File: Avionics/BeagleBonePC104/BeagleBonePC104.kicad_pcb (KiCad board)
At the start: 2 copper layers, 4 parts

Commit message: Ian Goldberg - Finished the footprint for the BeagleBonePCI104 Motherboard
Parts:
- added U2: ~, PCI104Connector:PCI104ConnectorAttempt#2H1, F.Cu at (80.0, 170.0)
- added U4: ~, PCI104Connector:PCI104ConnectorAttempt#2H2, F.Cu at (80.0, 170.0)
- moved U1 80.1 mm to (170.1, 90.8), turned to 180 degrees
- moved R1 63.2 mm to (113.0, 150.0)
- moved R2 51.1 mm to (126.5, 150.0)
- moved U3 21.6 mm to (110.1, 147.9), turned to 180 degrees
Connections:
- U1 pad 25: /GPIO3_21 -> /CAN_SLNT
- U3 pad 1: (no net) -> /3V3
- U3 pad 2: (no net) -> GND
- U3 pad 3: (no net) -> /CAN1_TX
- U3 pad 4: (no net) -> /CAN1_RX
- U3 pad 5: (no net) -> /CAN_SLNT
- U3 pad 6: (no net) -> /CAN_H
- U3 pad 7: (no net) -> /CAN_L
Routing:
- net GND: track 0.00 -> 2.54 mm
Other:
- board outline added: 90.2 x 95.9 mm

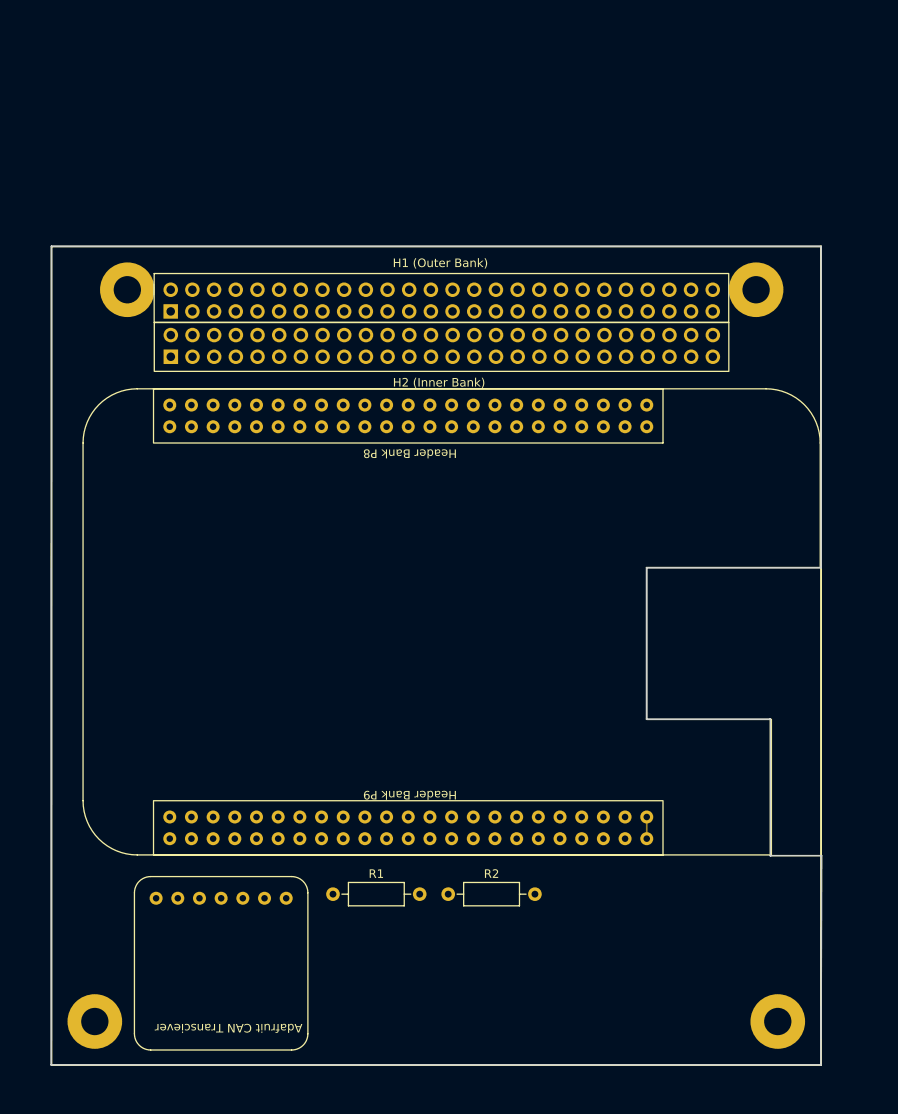
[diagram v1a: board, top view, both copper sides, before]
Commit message: Ian Goldberg - Finally finished the breakout board for the BeagleBone Black. Hoping to order the connectors soon and then asemble it.
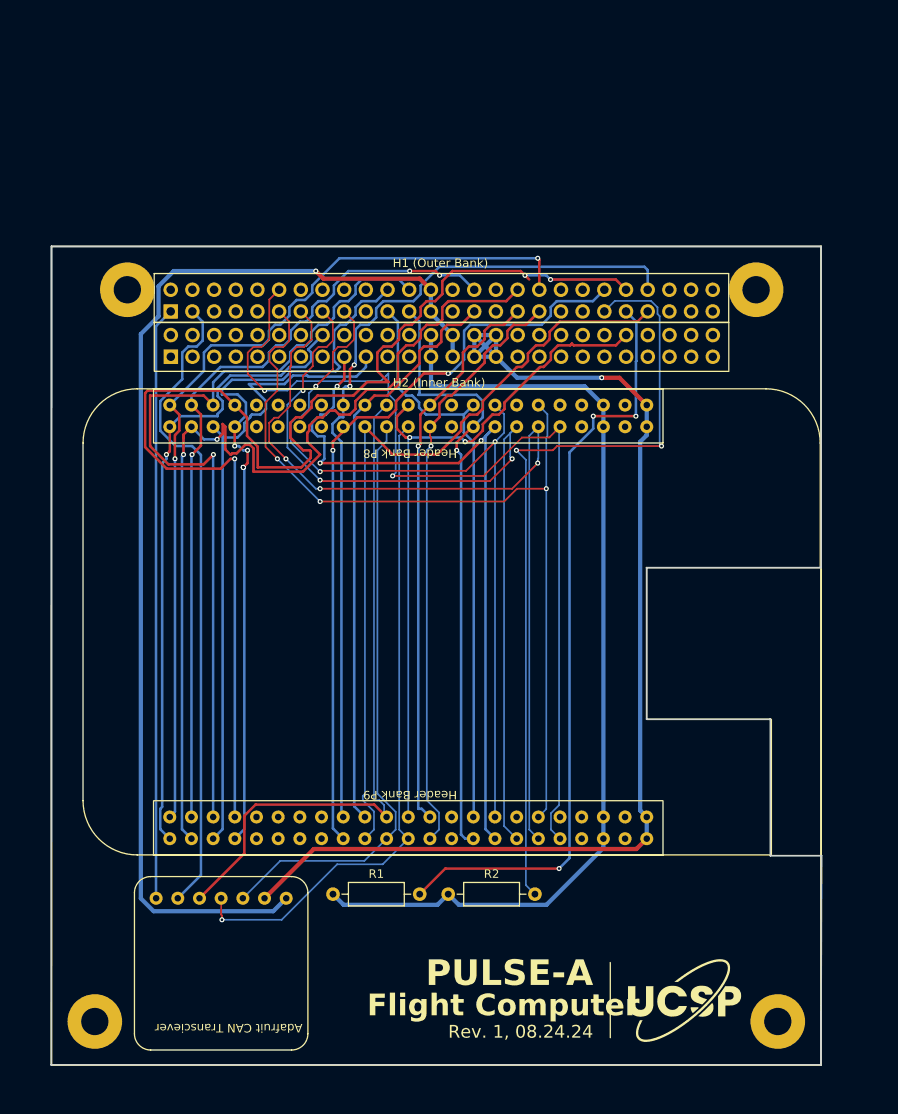
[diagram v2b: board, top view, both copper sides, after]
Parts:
- added G***: LOGO, LOGO, F.Cu at (154.0, 162.5)
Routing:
- net /GPIO2_12: track 0.00 -> 146.9 mm, vias 0 -> 3
- net GND: track 2.54 -> 136.5 mm, vias 0 -> 1
- net /3V3: track 0.00 -> 133.5 mm, vias 0 -> 1
- net /5V: track 0.00 -> 115.0 mm
- net /SYS_RESETn: track 0.00 -> 113.7 mm, vias 0 -> 2
- net /GPIO2_9: track 0.00 -> 112.7 mm, vias 0 -> 2
- net /GPIO1_12: track 0.00 -> 107.0 mm, vias 0 -> 3
- net /GPIO2_6: track 0.00 -> 106.1 mm, vias 0 -> 2
- net /GPIO1_13: track 0.00 -> 104.1 mm, vias 0 -> 3
- net /GPIO1_26: track 0.00 -> 102.0 mm, vias 0 -> 3
- net /GPIO2_23: track 0.00 -> 101.4 mm, vias 0 -> 2
- net /GPIO2_10: track 0.00 -> 98.9 mm, vias 0 -> 1
- net /GPIO1_15: track 0.00 -> 95.7 mm, vias 0 -> 3
- net /I2C_SDA: track 0.00 -> 93.6 mm, vias 0 -> 2
- net /GPIO2_24: track 0.00 -> 92.9 mm
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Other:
- board text added: "Flight Computer"
- board text added: "PULSE-A"
- board text added: "Rev. 1, 08.24.24"

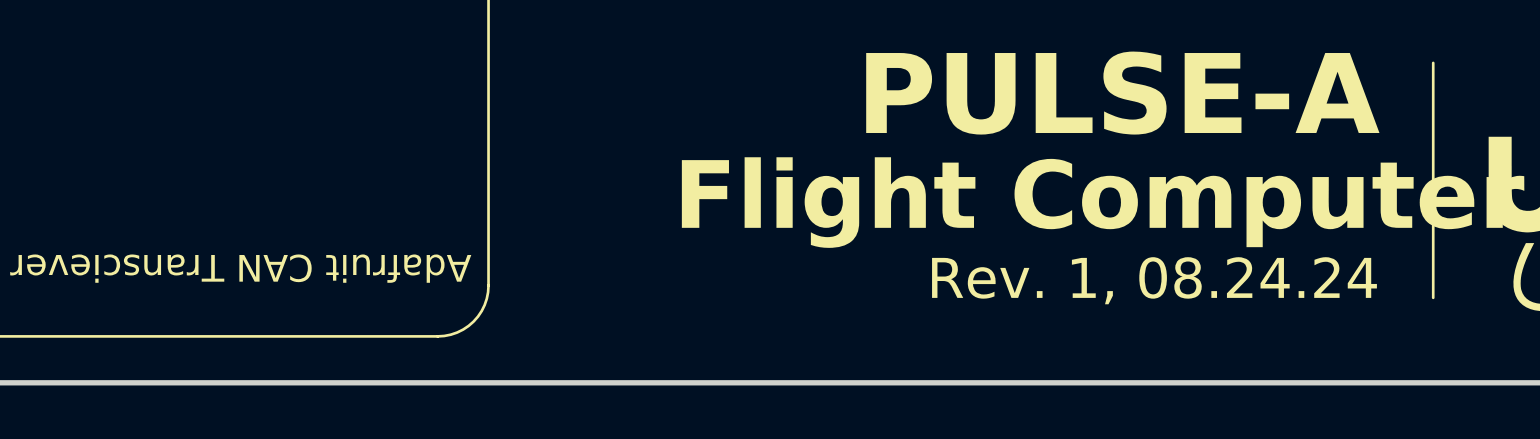
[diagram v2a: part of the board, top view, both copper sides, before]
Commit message: Ian Goldberg - pushed a correction to the BeagleBone Motherboard
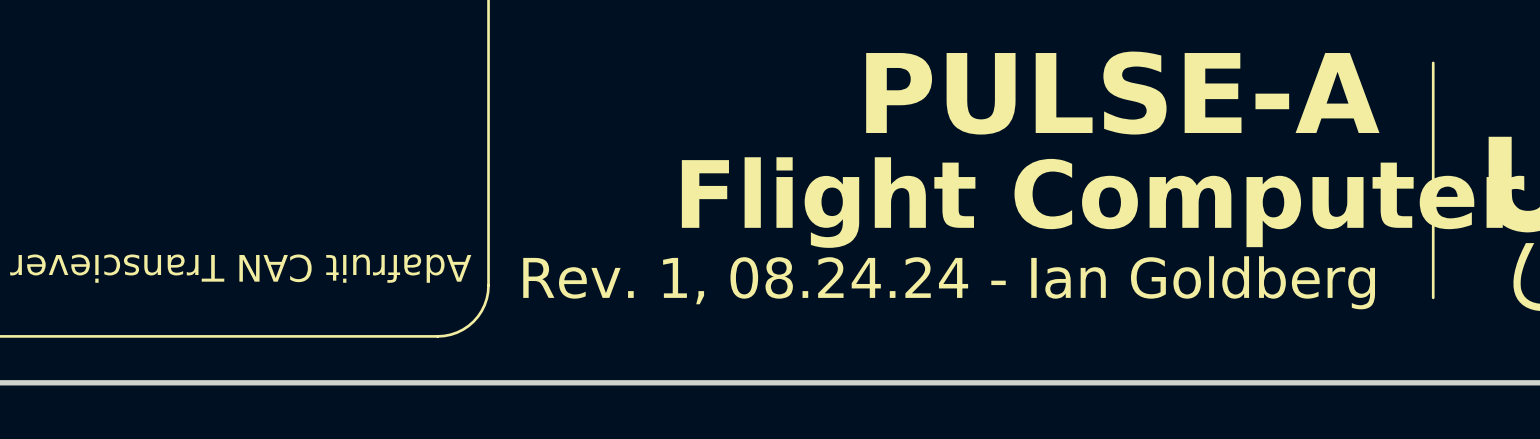
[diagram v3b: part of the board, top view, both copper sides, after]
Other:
- board text added: "Rev. 1, 08.24.24 - Ian Goldberg"
- board text removed: "Rev. 1, 08.24.24"

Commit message: Finally finished the BeagleBone Motherboard
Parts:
- moved G*** 1.12 mm to (154.5, 161.5)
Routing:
- net /GPIO2_6: track 106.1 -> 104.4 mm
- net /GPIO2_12: track 146.9 -> 145.8 mm
- net /GPIO2_13: vias 4 -> 3
- added copper zone on B.Cu, net GND
- added copper zone on F.Cu, net GND
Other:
- outline, holes or cut-outs redrawn
- board text added: "Rev. 1 - 08.24.24 - Ian Goldberg"
- board text added: "{dblquote}Do or do not, there is no try{dblquote} - Yoda"
- board text removed: "Rev. 1, 08.24.24 - Ian Goldberg"

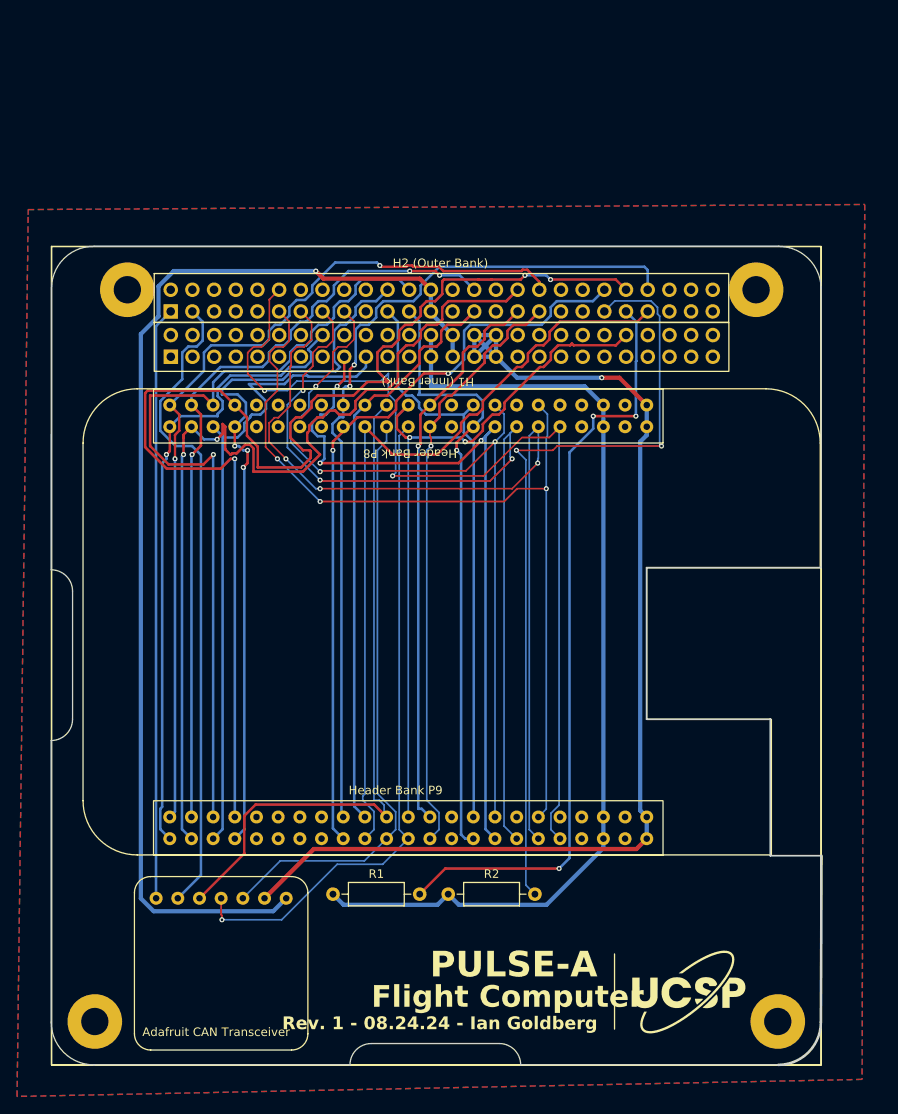
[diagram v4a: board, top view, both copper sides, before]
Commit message: Ian Goldberg - Finished Version 2 of the flight computer, added a temperature sensor to the board.
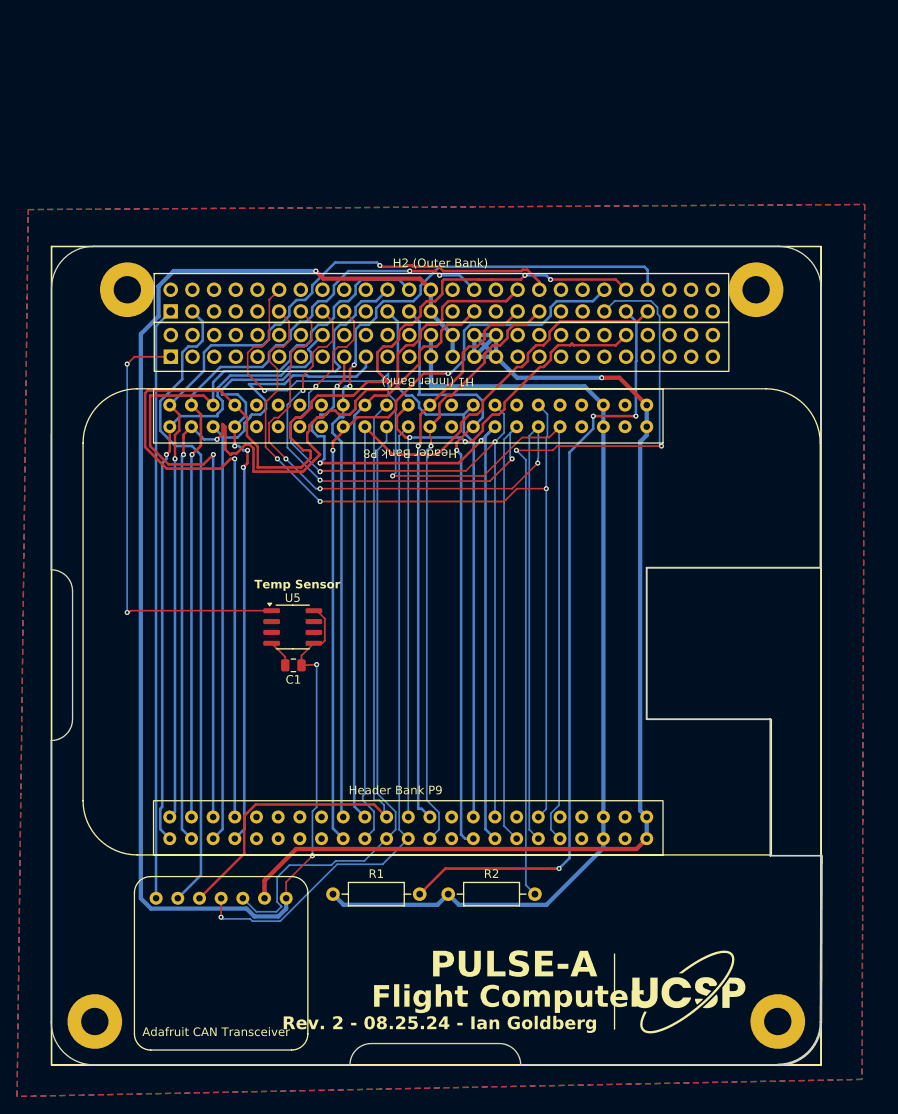
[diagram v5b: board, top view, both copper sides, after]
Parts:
- added C1: 0.1µF, Capacitor_SMD:C_0805_2012Metric, F.Cu at (108.4, 123.2)
- added U5: TMP36xS, Package_SO:SOIC-8_3.9x4.9mm_P1.27mm, F.Cu at (108.3, 118.7)
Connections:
- U4 pad 1: unconnected-(U4-TEMP_1-Pad1) -> /FC_TEMP
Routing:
- net /FC_TEMP: track 0.00 -> 51.6 mm, vias 0 -> 2
- net /3V3: track 133.5 -> 174.6 mm, vias 1 -> 3
- net GND: track 136.5 -> 140.9 mm
- net /CAN1_TX: track 69.8 -> 73.8 mm
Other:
- board text added: "Rev. 2 - 08.25.24 - Ian Goldberg"
- board text added: "Temp Sensor"
- board text added: "{dblquote}Do. Or do not. There is no try{dblquote} - Yoda"
- board text removed: "Rev. 1 - 08.24.24 - Ian Goldberg"
- board text removed: "{dblquote}Do or do not, there is no try{dblquote} - Yoda"
